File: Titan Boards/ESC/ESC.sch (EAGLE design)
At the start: 105 parts, among them IC2 74AHC1G08DBV, IC3 4002D, Q1 5.8A/30V/35mΩ, Q2 5.8A/30V/35mΩ, Q3 5.8A/30V/35mΩ, Q4 5.8A/30V/35mΩ, Q5 5.8A/30V/35mΩ, Q6 5.8A/30V/35mΩ, Q7 5.8A/30V/35mΩ, Q8 5.8A/30V/35mΩ

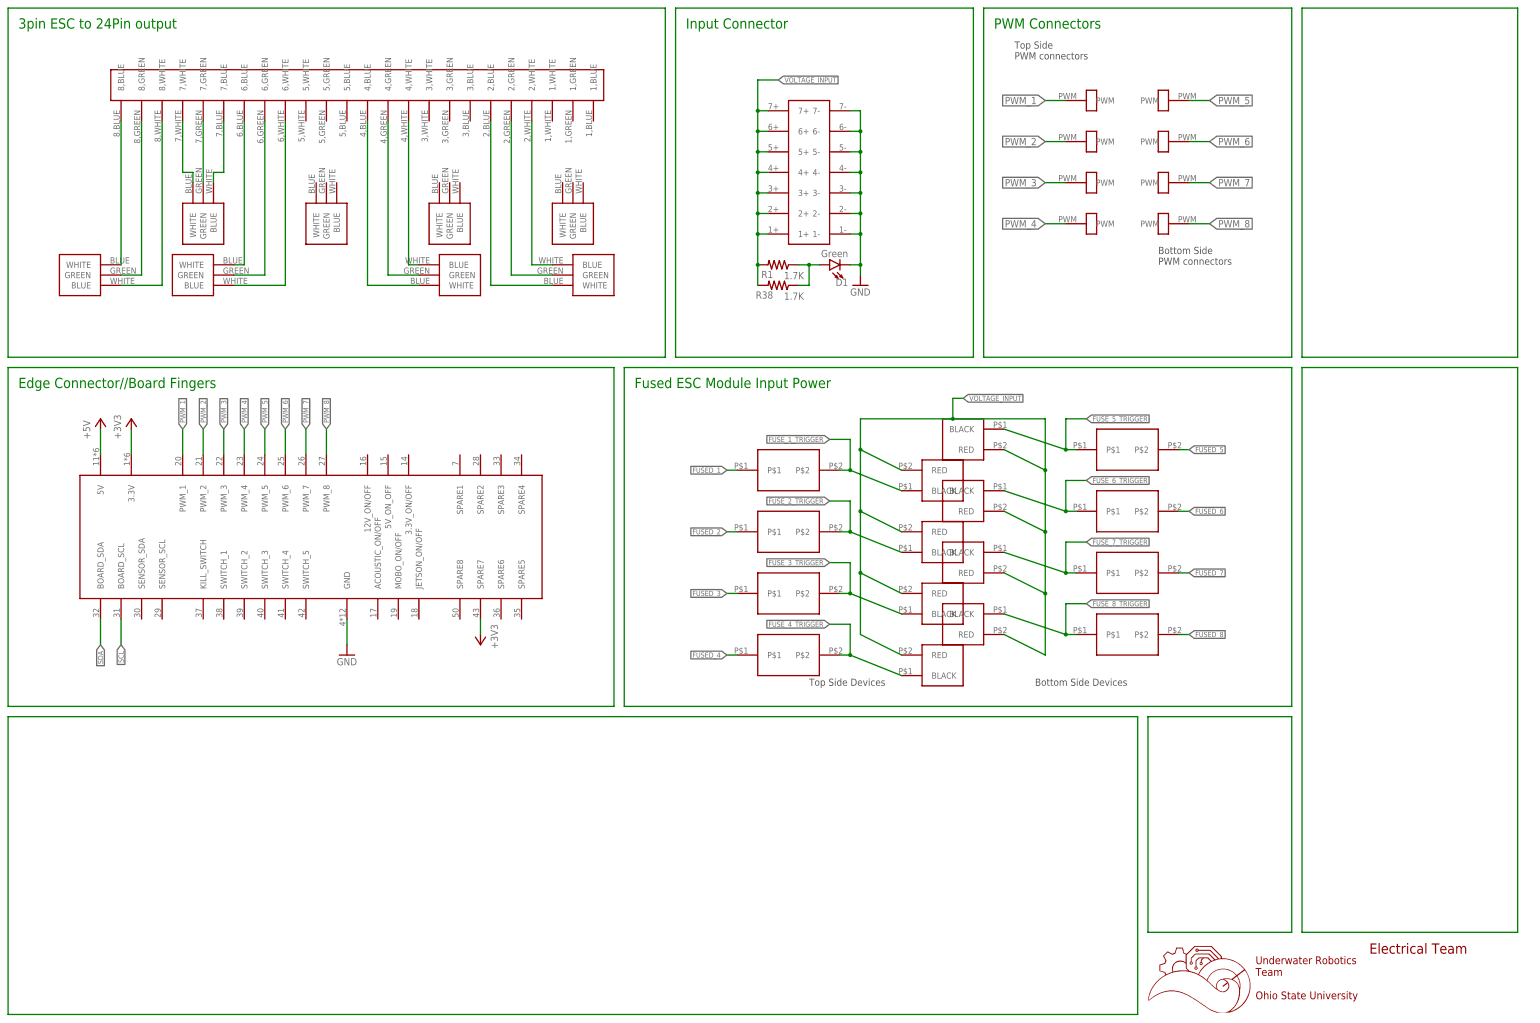
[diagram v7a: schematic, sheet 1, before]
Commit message: final commit for ESC board, resistor values changed across boards for order ease
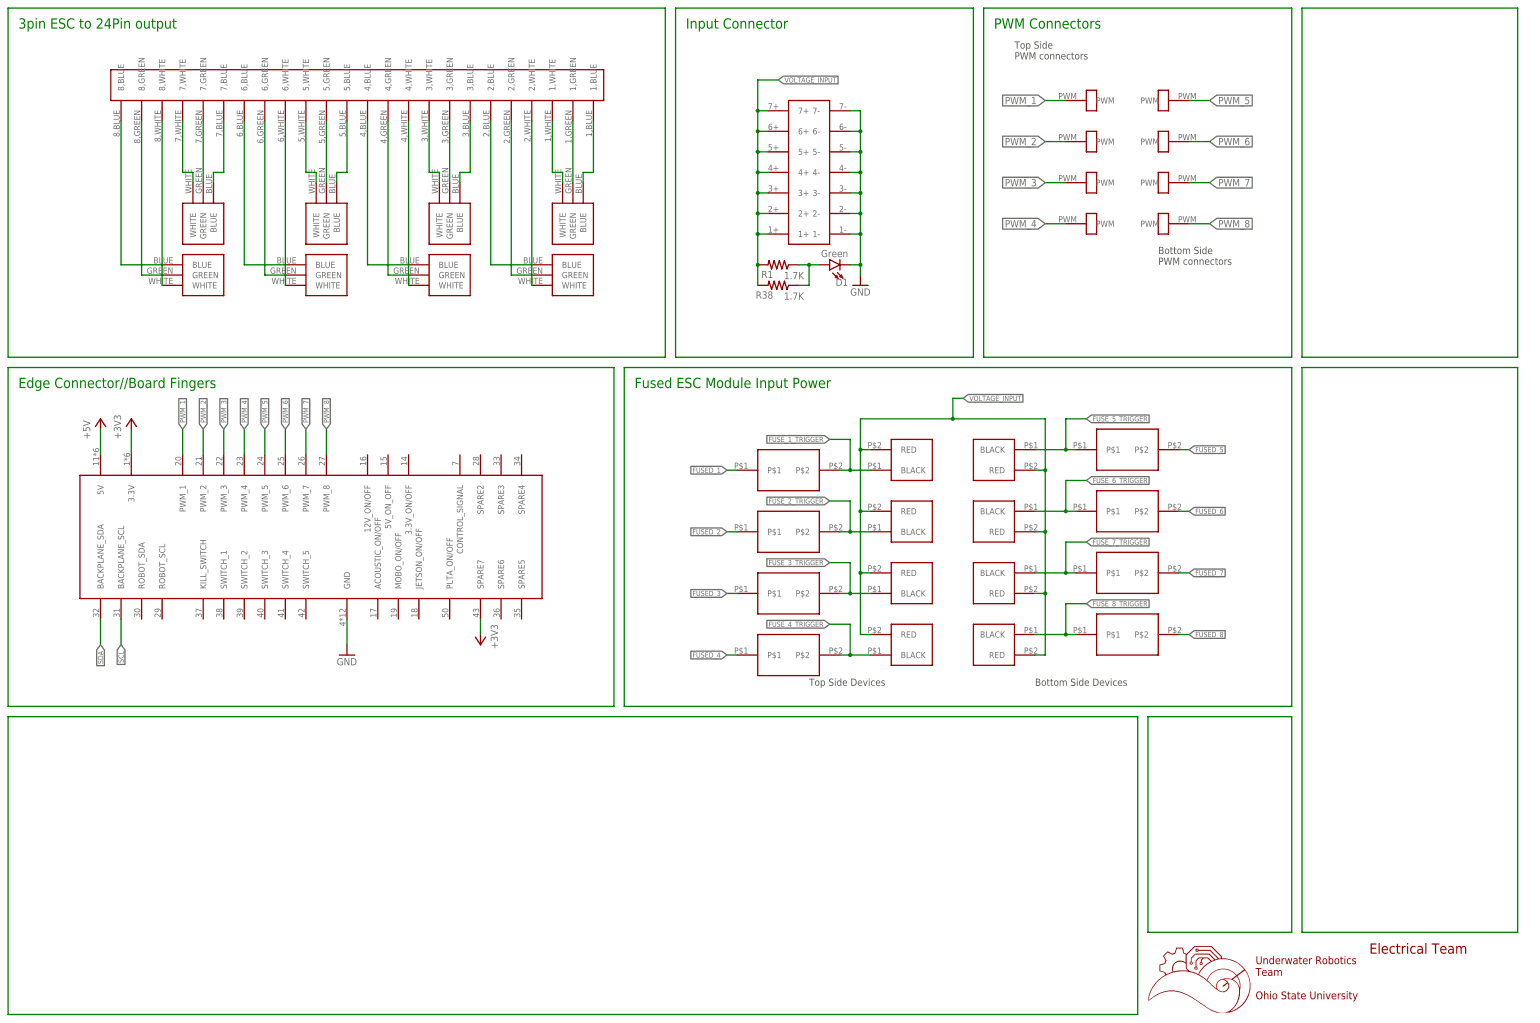
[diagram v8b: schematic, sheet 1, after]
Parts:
- R10, R11, R13, R14, R16, R17, R2, R20, R21, R23, R24, R3, R4, R5, R7, R8: value (none) -> 10k
- R28: value 91 -> 100
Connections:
- new net N$10: 24-PIN_CONNECTOR.5,WHITE, 3-PIN_2.WHITE
- new net N$11: 24-PIN_CONNECTOR.5,GREEN, 3-PIN_2.GREEN
- new net N$12: 24-PIN_CONNECTOR.5,BLUE, 3-PIN_2.BLUE
- new net N$13: 24-PIN_CONNECTOR.4,BLUE, 3-PIN_7.BLUE
- new net N$15: 24-PIN_CONNECTOR.4,WHITE, 3-PIN_7.WHITE
- new net N$16: 24-PIN_CONNECTOR.3,WHITE, 3-PIN_3.WHITE
- new net N$17: 24-PIN_CONNECTOR.3,GREEN, 3-PIN_3.GREEN
- new net N$18: 24-PIN_CONNECTOR.3,BLUE, 3-PIN_3.BLUE
- new net N$20: 24-PIN_CONNECTOR.1,BLUE, 3-PIN_4.BLUE
- net N$1: now also 3-PIN_5.BLUE; no longer 3-PIN_5.WHITE
- net N$19: now also 24-PIN_CONNECTOR.1,WHITE, 3-PIN_4.WHITE; no longer 24-PIN_CONNECTOR.4,WHITE, 3-PIN_7.BLUE
- net N$21: now also 24-PIN_CONNECTOR.1,GREEN, 3-PIN_4.GREEN; no longer 24-PIN_CONNECTOR.4,BLUE, 3-PIN_7.WHITE
- net N$22: now also 3-PIN_8.BLUE; no longer 3-PIN_8.WHITE
- net N$24: now also 3-PIN_8.WHITE; no longer 3-PIN_8.BLUE
- net N$3: now also 3-PIN_5.WHITE; no longer 3-PIN_5.BLUE
- net N$7: now also 3-PIN_6.BLUE; no longer 3-PIN_6.WHITE
- net N$9: now also 3-PIN_6.WHITE; no longer 3-PIN_6.BLUE
- net SCL: now also EDGE_CONNECTOR.BACKPLANE_SCL; no longer EDGE_CONNECTOR.BOARD_SCL
- net SDA: now also EDGE_CONNECTOR.BACKPLANE_SDA; no longer EDGE_CONNECTOR.BOARD_SDA
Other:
- note added: "2-Pin Terminal Block: Phoenix Contact 1755736 https://www.digikey.com/en/products/ detail/phoenix-contact/1755736/260518 https://media.digikey.com/pdf/Data%20Sheets/Phoenix%20Contact%20PDFs/ 1755736.pdf"
- note added: "3-Pin Terminal Block: Phoenix Contact 1755749 https://www.digikey.com/en/products/detail/phoenix-contact/1755749/260519? s=N4IgTCBcDaIIwHYCsSEBYCcIC6BfIA https://media.digikey.com/pdf/Data%20Sheets/Phoenix%20Contact%20PDFs/1755749.pdf"
- note removed: "2-Pin Terminal Block: Phoenix Contact 1711725 https://www.digikey.com/products/en?keywords=277-1027-ND%20 https://media.digikey.com/pdf/Data%20Sheets/Phoenix%20Contact%20PDFs/1711725.pdf"
- note removed: "3-Pin Terminal Block: Phoenix Contact 1711738 https://www.digikey.com/products/en?keywords=277-1028-ND%20 https://media.digikey.com/pdf/Data%20Sheets/Phoenix%20Contact%20PDFs/1711738.pdf"
